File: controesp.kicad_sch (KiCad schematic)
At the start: 27 parts, among them J14 Conn_01x16_Socket, J15 Screw_Terminal_01x02, J2 Screw_Terminal_01x04, J6 Screw_Terminal_01x04, J7 Screw_Terminal_01x04, J8 Screw_Terminal_01x04, U1 N7805-1PV, U5 LTV-847S, U6 LTV-847S

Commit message: merged seperate projects
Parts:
- removed D1, D2, D3, D4, D5, D6, D7, D8: LED, LED_SMD:LED_1206_3216Metric, symbol Device:LED
- removed J15: Screw_Terminal_01x02, symbol Connector:Screw_Terminal_01x02
- removed J6, J7: Screw_Terminal_01x04, symbol Connector:Screw_Terminal_01x04
- removed R1, R2, R3, R4, R5, R6, R7, R8: 1k, Resistor_SMD:R_0805_2012Metric, symbol Device:R
- removed R13: 10k, Resistor_SMD:R_0805_2012Metric, symbol Device:R
- removed R14: 15k, Resistor_SMD:R_0805_2012Metric, symbol Device:R
- removed U5, U6: LTV-847S, Package_DIP:SMDIP-16_W9.53mm, symbol Isolator:LTV-847S
- added J3: Conn_01x14_Socket, symbol Connector:Conn_01x14_Socket
- added J4: Conn_01x14_Pin, symbol Connector:Conn_01x14_Pin
- added J5: Conn_01x16_Pin, symbol Connector:Conn_01x16_Pin
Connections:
- net T2.O4 is gone; now on net +3V3: J14.9 (Pin_9)
- net +5V: now also J14.15 (Pin_15); no longer J14.1 (Pin_1)
- net GND: now also J14.12 (Pin_12), J4.13 (Pin_13), J4.14 (Pin_14)
- net input/SCL: now reaches J14.13 (Pin_13)
- net A1 renamed input/SDA
- net T1.O1 renamed input/DI2
- net T1.O2 renamed input/DI3
- net T1.O3 renamed input/DI4
- net T1.O4 renamed input/DI5
- net T2.O1 renamed input/DI6
- net T2.O2 renamed input/DI7
- net T2.O3 renamed input/DI8
- new net controesp_hat/13: J5.8 (Pin_8)
- new net controesp_hat/14: J5.6 (Pin_6)
- new net controesp_hat/25: J5.3 (Pin_3)
- new net controesp_hat/26: J5.4 (Pin_4)
- new net controesp_hat/27: J5.5 (Pin_5)
- new net controesp_hat/32: J5.1 (Pin_1)
- new net controesp_hat/33: J5.2 (Pin_2)
- new net controesp_hat/3V3: J5.9 (Pin_9)
- new net controesp_hat/5: J5.7 (Pin_7)
- new net controesp_hat/GND_hat: J5.16 (Pin_16)
- new net controesp_hat/P0: J4.1 (Pin_1)
- new net controesp_hat/P1: J4.2 (Pin_2)
- new net controesp_hat/P10: J4.9 (Pin_9)
- new net controesp_hat/P11: J4.10 (Pin_10)
- new net controesp_hat/P12: J4.11 (Pin_11)
- new net controesp_hat/P13: J4.12 (Pin_12)
- new net controesp_hat/P2: J4.3 (Pin_3)
- new net controesp_hat/P3: J4.4 (Pin_4)
- new net controesp_hat/P4: J4.5 (Pin_5)
- new net controesp_hat/P5: J4.6 (Pin_6)
- new net controesp_hat/P6: J4.7 (Pin_7)
- new net controesp_hat/P7: J4.8 (Pin_8)
- new net controesp_hat/RX2: J5.11 (Pin_11)
- new net controesp_hat/SCL: J5.13 (Pin_13)
- new net controesp_hat/SDA: J5.14 (Pin_14)
- new net controesp_hat/TX2: J5.10 (Pin_10)
- new net controesp_hat/VCC_hat: J5.15 (Pin_15)
- new net input/DI1: J14.1 (Pin_1)
- new net powerOutput/DO1: J3.1 (Pin_1)
- new net powerOutput/DO10: J3.10 (Pin_10)
- new net powerOutput/DO11: J3.11 (Pin_11)
- new net powerOutput/DO12: J3.12 (Pin_12)
- new net powerOutput/DO2: J3.2 (Pin_2)
- new net powerOutput/DO3: J3.3 (Pin_3)
- new net powerOutput/DO4: J3.4 (Pin_4)
- new net powerOutput/DO5: J3.5 (Pin_5)
- new net powerOutput/DO6: J3.6 (Pin_6)
- new net powerOutput/DO7: J3.7 (Pin_7)
- new net powerOutput/DO8: J3.8 (Pin_8)
- new net powerOutput/DO9: J3.9 (Pin_9)
- no-connect marks 0 -> 3
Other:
- added sheet controesp_hat (controesp_hat.kicad_sch)
- added sheet input (input.kicad_sch)
- sheet powerOutput ports: added COM, DO1, DO10, DO11, DO12, DO2, DO3, DO4, DO5, DO6, DO7, DO8, DO9, GND; removed none
- note removed: "Analog input 0-5V"
- note removed: "Digital input 1-4"
- note removed: "Digital input 5-8"
- moved on the sheet: J14, J8

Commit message: added part numbers
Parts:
- J14: footprint (none) -> Connector_PinSocket_2.54mm:PinSocket_1x16_P2.54mm_Vertical; LCSC (none) -> C66987
- J2, J8: footprint (none) -> Connector_Phoenix_MC:PhoenixContact_MC_1,5_4-G-3.5_1x04_P3.50mm_Horizontal; LCSC (none) -> C5241865
- J3: footprint (none) -> Connector_PinSocket_2.54mm:PinSocket_1x14_P2.54mm_Vertical; LCSC (none) -> C52711
- J4: footprint (none) -> Connector_PinHeader_2.54mm:PinHeader_1x14_P2.54mm_Vertical
- J5: footprint (none) -> Connector_PinHeader_2.54mm:PinHeader_1x16_P2.54mm_Vertical

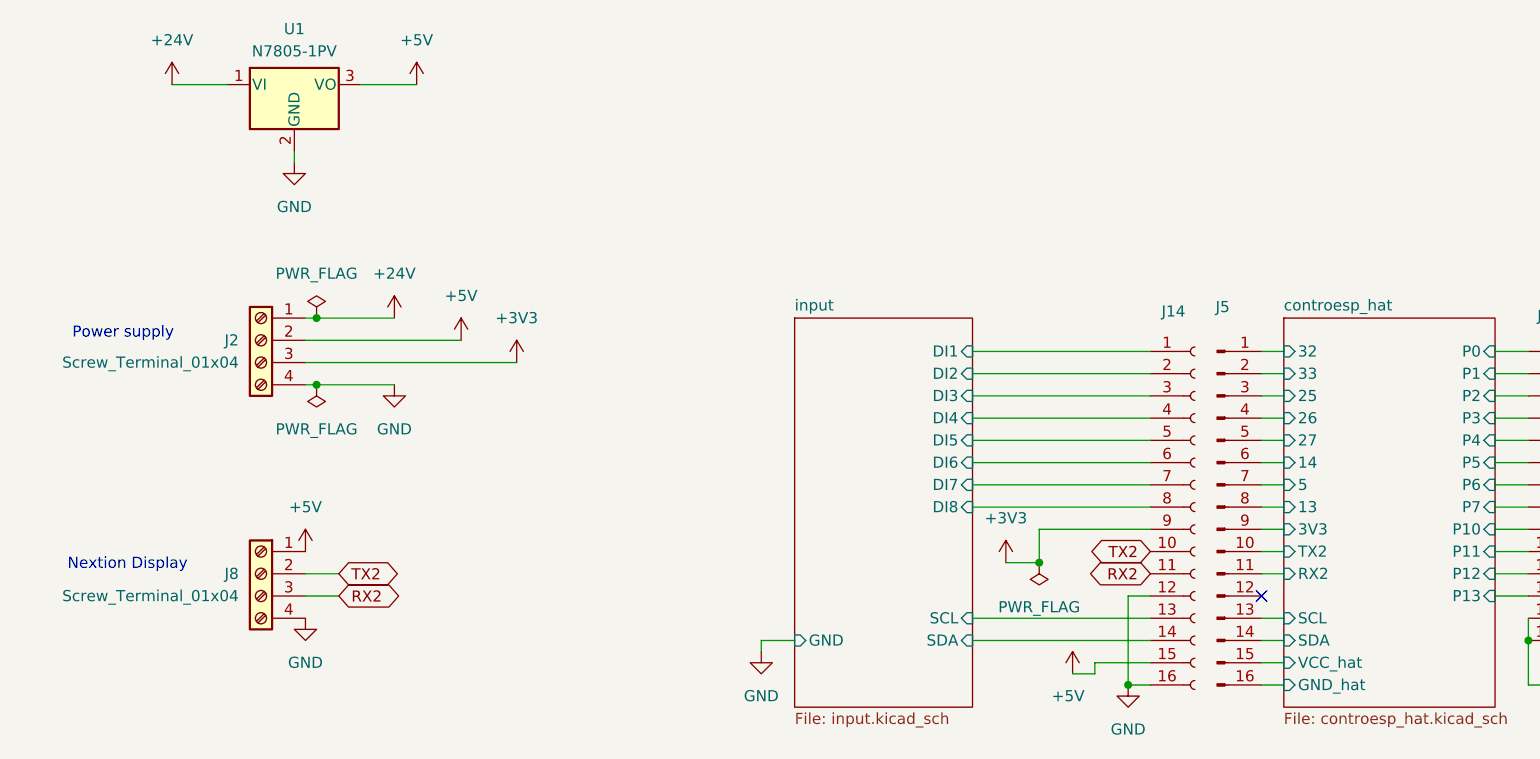
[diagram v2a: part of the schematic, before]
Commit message: added fuse and c for 7805
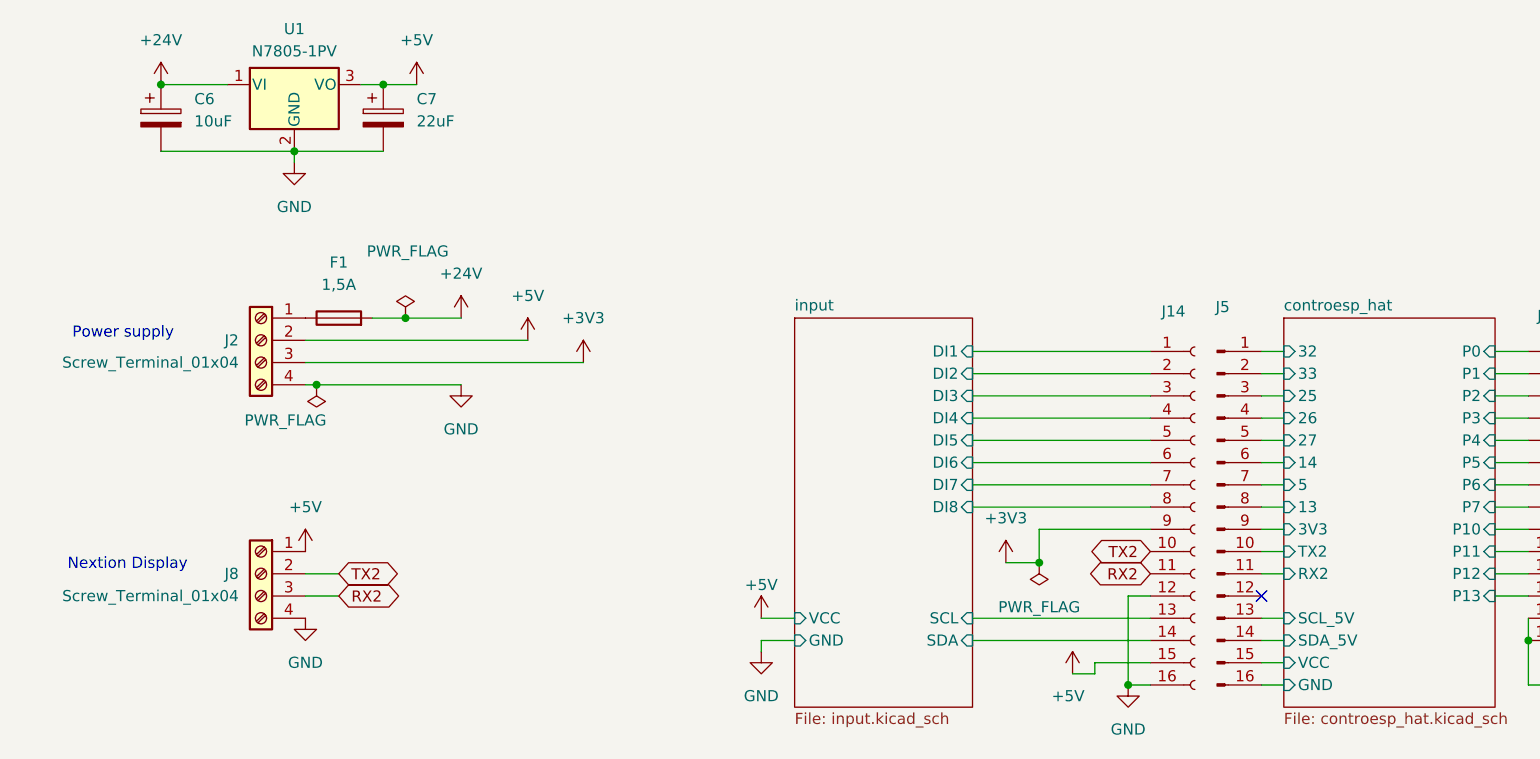
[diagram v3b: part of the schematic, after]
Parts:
- added C6: 10uF, Capacitor_Tantalum_SMD:CP_EIA-3216-12_Kemet-S_Pad1.58x1.35mm_HandSolder, symbol Device:C_Polarized
- added C7: 22uF, Capacitor_Tantalum_SMD:CP_EIA-2012-12_Kemet-R_Pad1.30x1.05mm_HandSolder, symbol Device:C_Polarized
- added F1: 1,5A, Fuse:Fuseholder_Littelfuse_Nano2_154x, symbol Device:Fuse
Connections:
- net +24V: now also C6.1, F1.2; no longer J2.1 (Pin_1)
- net +5V: now also C7.1
- net GND: now also C6.2, C7.2
- net controesp_hat/GND_hat renamed controesp_hat/GND
- net controesp_hat/SCL renamed controesp_hat/SCL_5V
- net controesp_hat/SDA renamed controesp_hat/SDA_5V
- net controesp_hat/VCC_hat renamed controesp_hat/VCC
- new net: F1.1, J2.1 (Pin_1)
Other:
- sheet controesp_hat ports: added GND, SCL_5V, SDA_5V, VCC; removed GND_hat, SCL, SDA, VCC_hat
- sheet input ports: added VCC; removed none

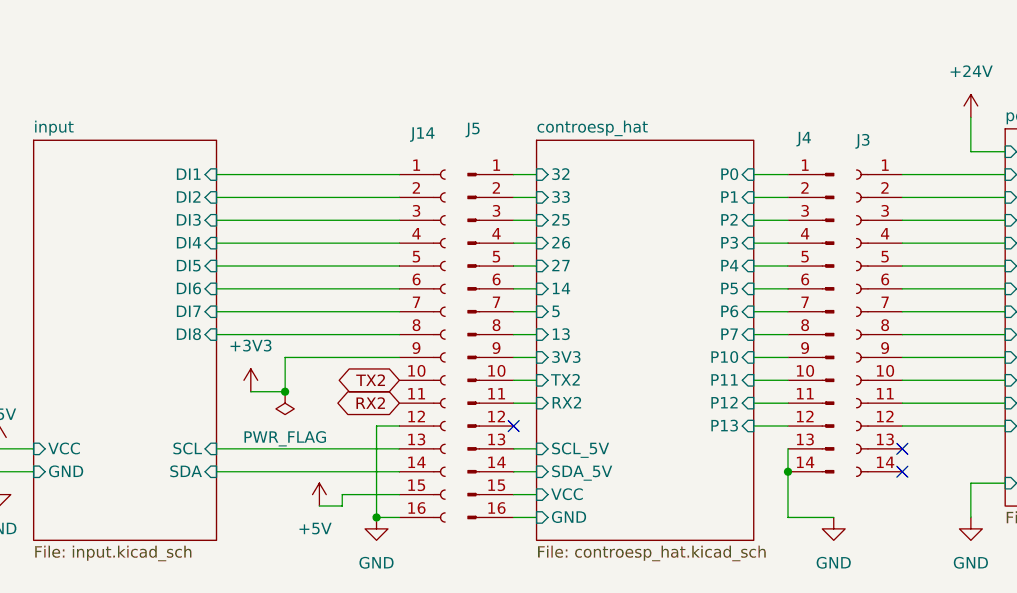
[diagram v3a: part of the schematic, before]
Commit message: hat routing finished
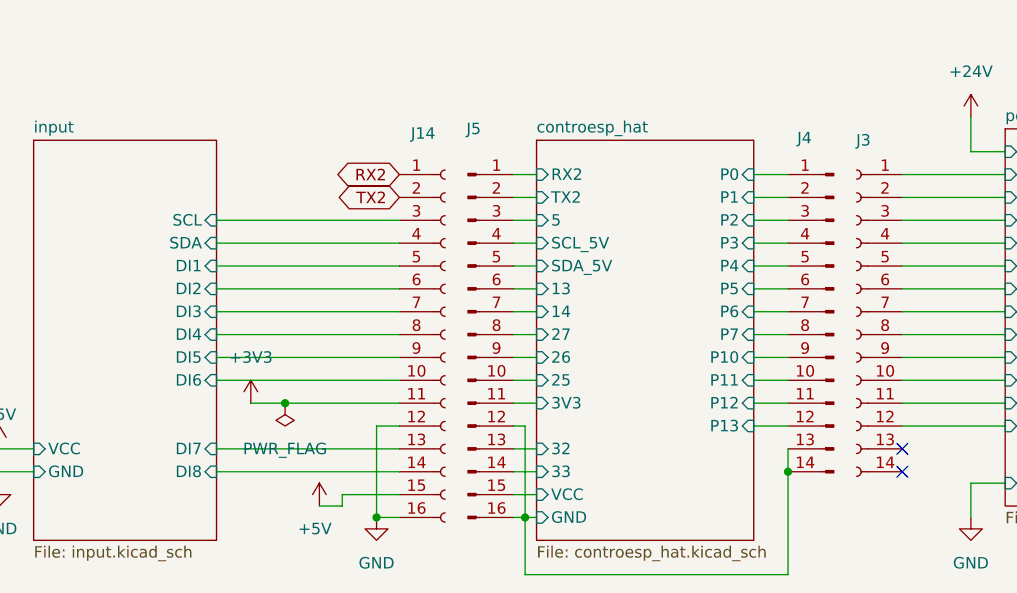
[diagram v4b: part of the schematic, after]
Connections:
- net +3V3: now also J14.11 (Pin_11); no longer J14.9 (Pin_9)
- net GND: no longer J4.13 (Pin_13), J4.14 (Pin_14)
- net RX2: now also J14.1 (Pin_1); no longer J14.11 (Pin_11)
- net TX2: now also J14.2 (Pin_2); no longer J14.10 (Pin_10)
- net controesp_hat/13: now also J5.6 (Pin_6); no longer J5.8 (Pin_8)
- net controesp_hat/14: now also J5.7 (Pin_7); no longer J5.6 (Pin_6)
- net controesp_hat/25: now also J5.10 (Pin_10); no longer J5.3 (Pin_3)
- net controesp_hat/26: now also J5.9 (Pin_9); no longer J5.4 (Pin_4)
- net controesp_hat/27: now also J5.8 (Pin_8); no longer J5.5 (Pin_5)
- net controesp_hat/32: now also J5.13 (Pin_13); no longer J5.1 (Pin_1)
- net controesp_hat/33: now also J5.14 (Pin_14); no longer J5.2 (Pin_2)
- net controesp_hat/3V3: now also J5.11 (Pin_11); no longer J5.9 (Pin_9)
- net controesp_hat/5: now also J5.3 (Pin_3); no longer J5.7 (Pin_7)
- net controesp_hat/GND: now also J4.13 (Pin_13), J4.14 (Pin_14), J5.12 (Pin_12)
- net controesp_hat/RX2: now also J5.1 (Pin_1); no longer J5.11 (Pin_11)
- net controesp_hat/SCL_5V: now also J5.4 (Pin_4); no longer J5.13 (Pin_13)
- net controesp_hat/SDA_5V: now also J5.5 (Pin_5); no longer J5.14 (Pin_14)
- net controesp_hat/TX2: now also J5.2 (Pin_2); no longer J5.10 (Pin_10)
- net input/DI1: now also J14.5 (Pin_5); no longer J14.1 (Pin_1)
- net input/DI2: now also J14.6 (Pin_6); no longer J14.2 (Pin_2)
- net input/DI3: now also J14.7 (Pin_7); no longer J14.3 (Pin_3)
- net input/DI4: now also J14.8 (Pin_8); no longer J14.4 (Pin_4)
- net input/DI5: now also J14.9 (Pin_9); no longer J14.5 (Pin_5)
- net input/DI6: now also J14.10 (Pin_10); no longer J14.6 (Pin_6)
- net input/DI7: now also J14.13 (Pin_13); no longer J14.7 (Pin_7)
- net input/DI8: now also J14.14 (Pin_14); no longer J14.8 (Pin_8)
- net input/SCL: now also J14.3 (Pin_3); no longer J14.13 (Pin_13)
- net input/SDA: now also J14.4 (Pin_4); no longer J14.14 (Pin_14)
- no-connect marks 3 -> 2

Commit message: von ben
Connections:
- net RX2: now also J14.13 (Pin_13), J8.2 (Pin_2); no longer J14.1 (Pin_1), J8.3 (Pin_3)
- net TX2: now also J14.14 (Pin_14), J8.3 (Pin_3); no longer J14.2 (Pin_2), J8.2 (Pin_2)
- net controesp_hat/25: no longer J5.10 (Pin_10)
- net controesp_hat/26: no longer J5.9 (Pin_9)
- net controesp_hat/32: now also J5.1 (Pin_1); no longer J5.13 (Pin_13)
- net controesp_hat/33: now also J5.2 (Pin_2); no longer J5.14 (Pin_14)
- net controesp_hat/RX2: now also J5.13 (Pin_13); no longer J5.1 (Pin_1)
- net controesp_hat/SCL_5V: now also J5.10 (Pin_10); no longer J5.4 (Pin_4)
- net controesp_hat/SDA_5V: now also J5.9 (Pin_9); no longer J5.5 (Pin_5)
- net controesp_hat/TX2: now also J5.14 (Pin_14); no longer J5.2 (Pin_2)
- net input/DI1: now also J14.1 (Pin_1); no longer J14.5 (Pin_5)
- net input/DI2: now also J14.2 (Pin_2); no longer J14.6 (Pin_6)
- net input/DI3: now also J14.5 (Pin_5); no longer J14.7 (Pin_7)
- net input/DI4: now also J14.6 (Pin_6); no longer J14.8 (Pin_8)
- net input/DI5: now also J14.7 (Pin_7); no longer J14.9 (Pin_9)
- net input/DI6: now also J14.8 (Pin_8); no longer J14.10 (Pin_10)
- net input/DI7: now also J14.4 (Pin_4); no longer J14.13 (Pin_13)
- net input/DI8: now also J14.3 (Pin_3); no longer J14.14 (Pin_14)
- net input/SCL: now also J14.10 (Pin_10); no longer J14.3 (Pin_3)
- net input/SDA: now also J14.9 (Pin_9); no longer J14.4 (Pin_4)
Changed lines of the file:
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@@
 	(wire
 		(pts
-			(xy 119.38 87.63) (xy 139.7 87.63)
+			(xy 119.38 57.15) (xy 139.7 57.15)
 		)
 		(stroke
@@
 	(wire
 		(pts
-			(xy 119.38 74.93) (xy 139.7 74.93)
+			(xy 119.38 77.47) (xy 139.7 77.47)
 		)
 		(stroke
@@
 	(wire
 		(pts
-			(xy 119.38 85.09) (xy 139.7 85.09)
+			(xy 119.38 54.61) (xy 139.7 54.61)
 		)
 		(stroke
@@
 	(wire
 		(pts
-			(xy 119.38 77.47) (xy 139.7 77.47)
+			(xy 119.38 74.93) (xy 139.7 74.93)
 		)
 		(stroke
@@
 	(global_label "RX2"
 		(shape bidirectional)
-		(at 139.7 54.61 180)
+		(at 139.7 85.09 180)
 		(fields_autoplaced yes)
 		(effects
@@
 		)
 		(property "Intersheetrefs" "${INTERSHEET_REFS}"
-			(at 131.9145 54.61 0)
+			(at 131.9145 85.09 0)
 			(effects
 				(font
@@
 	(global_label "TX2"
 		(shape bidirectional)
-		(at 139.7 57.15 180)
+		(at 139.7 87.63 180)
 		(fields_autoplaced yes)
 		(effects
@@
 		)
 		(property "Intersheetrefs" "${INTERSHEET_REFS}"
-			(at 132.2169 57.15 0)
+			(at 132.2169 87.63 0)
 			(effects
 				(font
@@
 	(global_label "RX2"
 		(shape bidirectional)
-		(at 46.99 82.55 0)
+		(at 46.99 80.01 0)
 		(fields_autoplaced yes)
 		(effects
@@
 		)
 		(property "Intersheetrefs" "${INTERSHEET_REFS}"
-			(at 54.7755 82.55 0)
+			(at 54.7755 80.01 0)
 			(effects
 				(font
@@
 	(global_label "TX2"
 		(shape bidirectional)
-		(at 46.99 80.01 0)
+		(at 46.99 82.55 0)
 		(fields_autoplaced yes)
 		(effects
@@
 		)
 		(property "Intersheetrefs" "${INTERSHEET_REFS}"
-			(at 54.4731 80.01 0)
+			(at 54.4731 82.55 0)
 			(effects
 				(font
@@
 		)
 		(pin "DI1" input
-			(at 119.38 64.77 0)
+			(at 119.38 54.61 0)
 			(effects
 				(font
@@
 		)
 		(pin "DI2" input
-			(at 119.38 67.31 0)
+			(at 119.38 57.15 0)
 			(effects
 				(font
@@
 		)
 		(pin "DI3" input
-			(at 119.38 69.85 0)
+			(at 119.38 64.77 0)
 			(effects
 				(font
@@
 		)
 		(pin "DI4" input
-			(at 119.38 72.39 0)
+			(at 119.38 67.31 0)
 			(effects
 				(font
@@
 		)
 		(pin "DI5" input
-			(at 119.38 74.93 0)
+			(at 119.38 69.85 0)
 			(effects
 				(font
@@
 		)
 		(pin "DI6" input
-			(at 119.38 77.47 0)
+			(at 119.38 72.39 0)
 			(effects
 				(font
@@
 		)
 		(pin "DI7" input
-			(at 119.38 85.09 0)
+			(at 119.38 62.23 0)
 			(effects
 				(font
@@
 		)
 		(pin "DI8" input
-			(at 119.38 87.63 0)
+			(at 119.38 59.69 0)
 			(effects
 				(font
@@
 		)
 		(pin "SCL" input
-			(at 119.38 59.69 0)
+			(at 119.38 77.47 0)
 			(effects
 				(font
@@
 		)
 		(pin "SDA" input
-			(at 119.38 62.23 0)
+			(at 119.38 74.93 0)
 			(effects
 				(font
@@
 		)
 		(pin "32" input
-			(at 154.94 85.09 180)
+			(at 154.94 54.61 180)
 			(effects
 				(font
@@
 		)
 		(pin "RX2" input
-			(at 154.94 54.61 180)
+			(at 154.94 85.09 180)
 			(effects
 				(font
@@
 		)
 		(pin "TX2" input
-			(at 154.94 57.15 180)
+			(at 154.94 87.63 180)
 			(effects
 				(font
@@
 		)
 		(pin "33" input
-			(at 154.94 87.63 180)
+			(at 154.94 57.15 180)
 			(effects
 				(font
@@
 		)
 		(pin "25" input
-			(at 154.94 77.47 180)
+			(at 166.37 50.8 90)
 			(effects
 				(font
 					(size 1.27 1.27)
 				)
-				(justify left)
+				(justify right)
 			)
 		)
 		(pin "26" input
-			(at 154.94 74.93 180)
+			(at 168.91 50.8 90)
 			(effects
 				(font
 					(size 1.27 1.27)
 				)
-				(justify left)
+				(justify right)
 			)
 		)
@@
 		)
 		(pin "SCL_5V" input
-			(at 154.94 62.23 180)
+			(at 154.94 77.47 180)
 			(effects
 				(font
@@
 		)
 		(pin "SDA_5V" input
-			(at 154.94 64.77 180)
+			(at 154.94 74.93 180)
 			(effects
 				(font
